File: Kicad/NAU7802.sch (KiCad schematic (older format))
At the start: 19 parts, among them J1 A Scale, J2 B scale, J3 I²C, J4 Scale, J5 AVDD, J6 INT, U1 NAU7802SGI

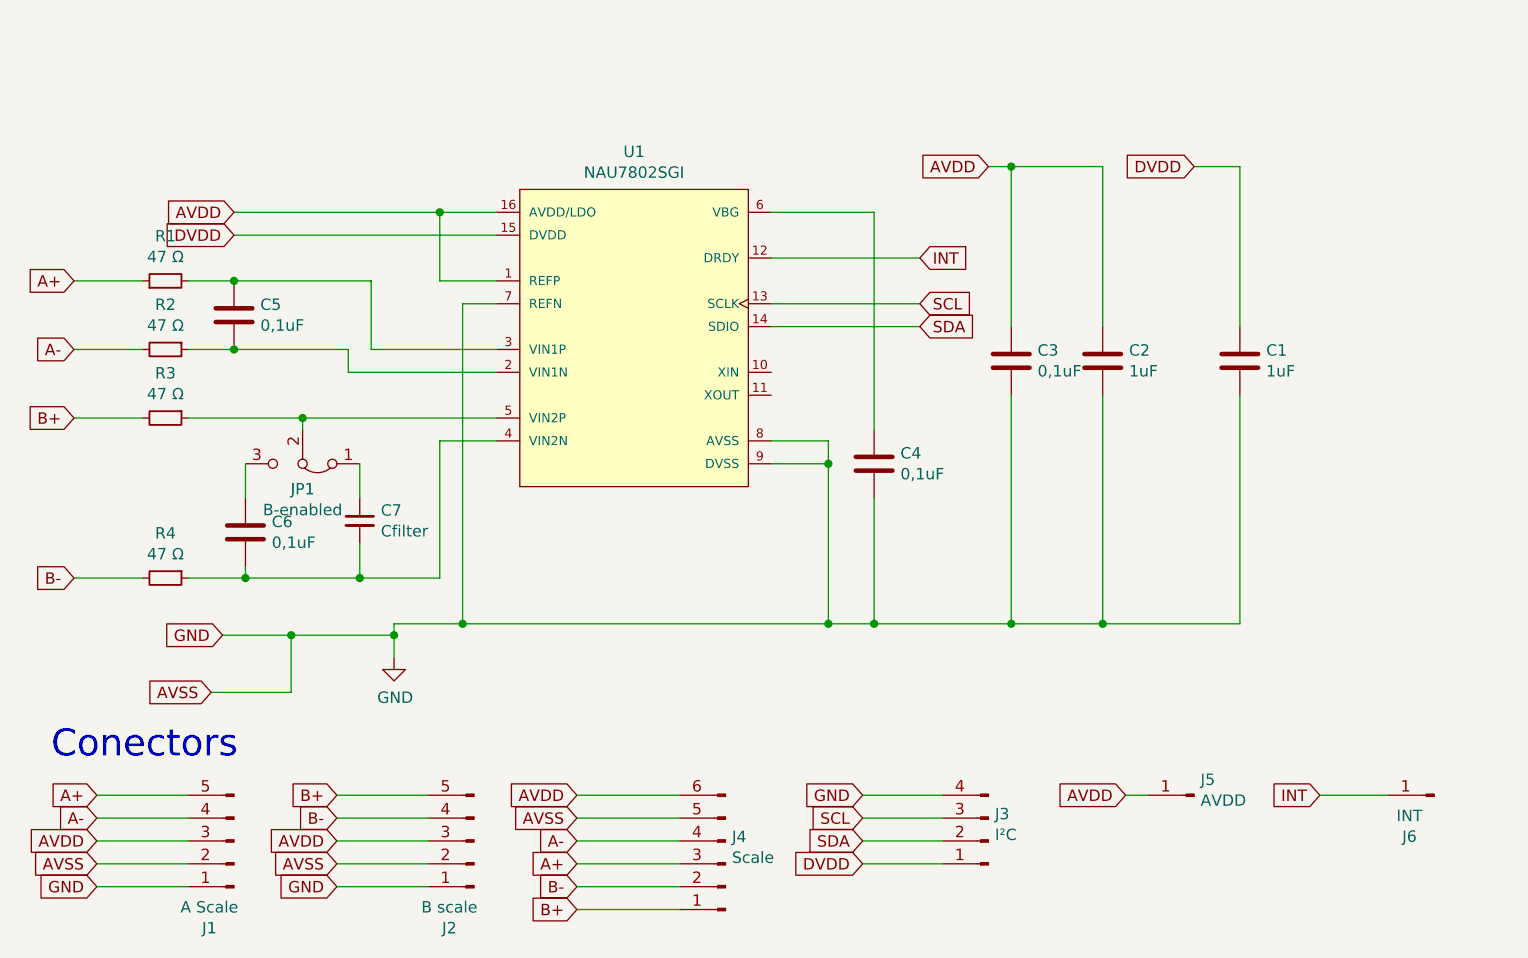
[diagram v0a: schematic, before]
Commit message: ADD I²C Pullup + Jumper
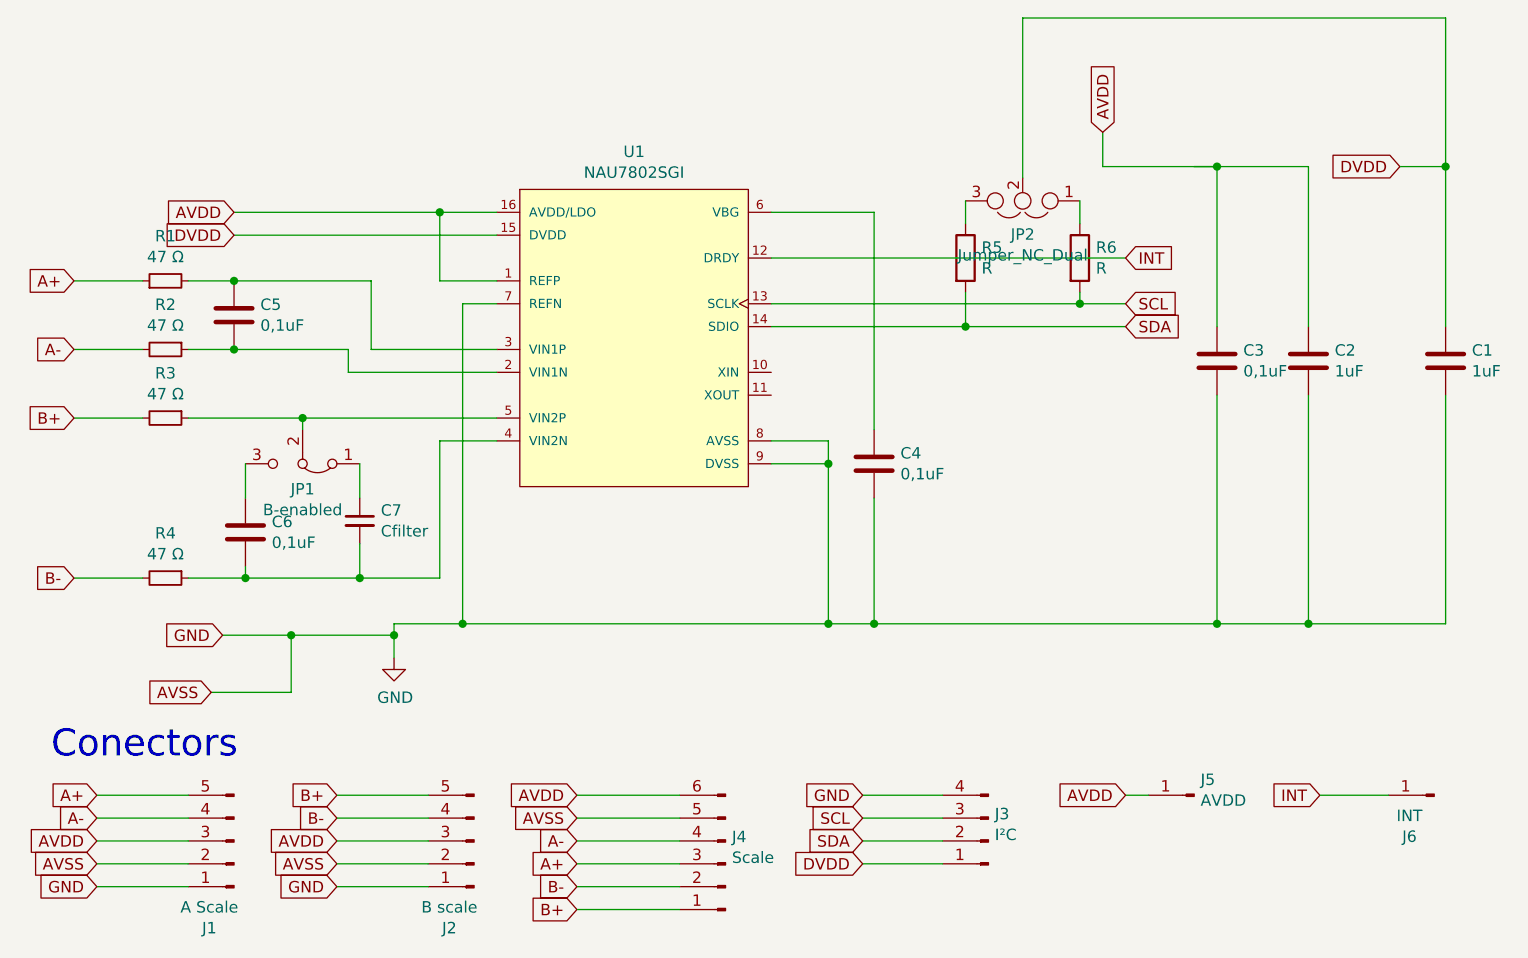
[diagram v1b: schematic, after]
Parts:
- added JP2: Jumper_NC_Dual, Jumper:SolderJumper-3_P1.3mm_Open_RoundedPad1.0x1.5mm, symbol Device:Jumper_NC_Dual
- added R5, R6: R, Resistor_SMD:R_0805_2012Metric, symbol Device:R
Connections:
- net DVDD: now also JP2.2
- net SCL: now also R6.2
- net SDA: now also R5.2
- new net: JP2.1, R6.1
- new net: JP2.3, R5.1
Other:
- moved on the sheet: C1, C2, C3
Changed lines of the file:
@@
 L Device:C C2
 U 1 1 5F00379D
-P 6850 3550
-F 0 "C2" H 6965 3596 50  0000 L CNN
-F 1 "1uF" H 6965 3505 50  0000 L CNN
-F 2 "Capacitor_SMD:C_0805_2012Metric" H 6888 3400 50  0001 C CNN
-F 3 "~" H 6850 3550 50  0001 C CNN
-	1    6850 3550
+P 7750 3550
+F 0 "C2" H 7865 3596 50  0000 L CNN
+F 1 "1uF" H 7865 3505 50  0000 L CNN
+F 2 "Capacitor_SMD:C_0805_2012Metric" H 7788 3400 50  0001 C CNN
+F 3 "~" H 7750 3550 50  0001 C CNN
+	1    7750 3550
 	1    0    0    -1
 $EndComp
@@
 L Device:C C1
 U 1 1 5F003FEF
-P 7450 3550
-F 0 "C1" H 7565 3596 50  0000 L CNN
-F 1 "1uF" H 7565 3505 50  0000 L CNN
-F 2 "Capacitor_SMD:C_0805_2012Metric" H 7488 3400 50  0001 C CNN
-F 3 "~" H 7450 3550 50  0001 C CNN
-	1    7450 3550
+P 8350 3550
+F 0 "C1" H 8465 3596 50  0000 L CNN
+F 1 "1uF" H 8465 3505 50  0000 L CNN
+F 2 "Capacitor_SMD:C_0805_2012Metric" H 8388 3400 50  0001 C CNN
+F 3 "~" H 8350 3550 50  0001 C CNN
+	1    8350 3550
 	1    0    0    -1
 $EndComp
@@
 Wire Wire Line
 	3500 5850 3900 5850
-Text GLabel 6050 3400 2    50   Input ~ 0
+Text GLabel 6950 3400 2    50   Input ~ 0
 SDA
-Text GLabel 6050 3300 2    50   Input ~ 0
+Text GLabel 6950 3300 2    50   Input ~ 0
 SCL
-Text GLabel 6050 3100 2    50   Input ~ 0
+Text GLabel 6950 3100 2    50   Input ~ 0
 INT
 Wire Wire Line
@@
 Wire Wire Line
 	5400 4000 5650 4000
-Wire Wire Line
-	5400 3100 6050 3100
-Wire Wire Line
-	5400 3300 6050 3300
-Wire Wire Line
-	5400 3400 6050 3400
 $Comp
 L Device:C C3
 U 1 1 5F05C52D
-P 6450 3550
-F 0 "C3" H 6565 3596 50  0000 L CNN
-F 1 "0,1uF" H 6565 3505 50  0000 L CNN
-F 2 "Capacitor_SMD:C_0805_2012Metric" H 6488 3400 50  0001 C CNN
-F 3 "~" H 6450 3550 50  0001 C CNN
-	1    6450 3550
-	1    0    0    -1
-$EndComp
-Text GLabel 6350 2700 0    50   Input ~ 0
+P 7350 3550
+F 0 "C3" H 7465 3596 50  0000 L CNN
+F 1 "0,1uF" H 7465 3505 50  0000 L CNN
+F 2 "Capacitor_SMD:C_0805_2012Metric" H 7388 3400 50  0001 C CNN
+F 3 "~" H 7350 3550 50  0001 C CNN
+	1    7350 3550
+	1    0    0    -1
+$EndComp
+Text GLabel 6850 2550 1    50   Input ~ 0
 AVDD
-Text GLabel 7250 2700 0    50   Input ~ 0
+Text GLabel 8150 2700 0    50   Input ~ 0
 DVDD
 Wire Wire Line
-	6350 2700 6450 2700
-Wire Wire Line
-	6450 2700 6450 3400
-Wire Wire Line
-	6850 2700 6850 3400
-Connection ~ 5850 4700
+	7350 2700 7350 3400
+Wire Wire Line
+	7750 2700 7750 3400
 Text GLabel 5800 5750 0    50   Input ~ 0
 DVDD
@@
 Wire Wire Line
 	4550 5950 5000 5950
-Connection ~ 6450 2700
-Connection ~ 6450 4700
-Wire Wire Line
-	5850 4700 6450 4700
-Connection ~ 6850 4700
-Wire Wire Line
-	6450 4700 6850 4700
-Wire Wire Line
-	7250 2700 7450 2700
-Wire Wire Line
-	7450 2700 7450 3400
-Wire Wire Line
-	6450 2700 6850 2700
-Wire Wire Line
-	6850 4700 7450 4700
+Connection ~ 7350 2700
+Connection ~ 7350 4700
+Connection ~ 7750 4700
+Wire Wire Line
+	7350 4700 7750 4700
+Wire Wire Line
+	8150 2700 8350 2700
+Wire Wire Line
+	8350 2700 8350 3400
+Wire Wire Line
+	7350 2700 7750 2700
+Wire Wire Line
+	7750 4700 8350 4700
 Wire Wire Line
 	3050 3000 4200 3000
@@
 Connection ~ 5650 4000
 Wire Wire Line
-	6450 3700 6450 4700
-Wire Wire Line
-	6850 3700 6850 4700
-Wire Wire Line
-	7450 3700 7450 4700
+	7350 3700 7350 4700
+Wire Wire Line
+	7750 3700 7750 4700
+Wire Wire Line
+	8350 3700 8350 4700
 Wire Wire Line
 	4050 4700 5650 4700
@@
 Wire Wire Line
 	3350 3800 4200 3800
+Wire Wire Line
+	5850 4700 7350 4700
+Connection ~ 5850 4700
+Wire Wire Line
+	5400 3100 6950 3100
+$Comp
+L Device:Jumper_NC_Dual JP2
+U 1 1 5F0512F0
+P 6500 2850
+F 0 "JP2" H 6500 2997 50  0000 C CNN
+F 1 "Jumper_NC_Dual" H 6500 3088 50  0000 C CNN
+F 2 "Jumper:SolderJumper-3_P1.3mm_Open_RoundedPad1.0x1.5mm" H 6500 2850 50  0001 C CNN
+F 3 "~" H 6500 2850 50  0001 C CNN
+	1    6500 2850
+	-1   0    0    1
+$EndComp
+Wire Wire Line
+	6500 2750 6500 2050
+Wire Wire Line
+	6500 2050 8350 2050
+Wire Wire Line
+	8350 2050 8350 2700
+Connection ~ 8350 2700
+Wire Wire Line
+	6850 2550 6850 2700
+$Comp
+L Device:R R5
+U 1 1 5F05ACB5
+P 6250 3100
+F 0 "R5" H 6320 3146 50  0000 L CNN
+F 1 "R" H 6320 3055 50  0000 L CNN
+F 2 "Resistor_SMD:R_0805_2012Metric" V 6180 3100 50  0001 C CNN
+F 3 "~" H 6250 3100 50  0001 C CNN
+	1    6250 3100
+	1    0    0    -1
+$EndComp
+$Comp
+L Device:R R6
+U 1 1 5F05BCD1
+P 6750 3100
+F 0 "R6" H 6820 3146 50  0000 L CNN
+F 1 "R" H 6820 3055 50  0000 L CNN
+F 2 "Resistor_SMD:R_0805_2012Metric" V 6680 3100 50  0001 C CNN
+F 3 "~" H 6750 3100 50  0001 C CNN
+	1    6750 3100
+	1    0    0    -1
+$EndComp
+Wire Wire Line
+	5400 3300 6750 3300
+Wire Wire Line
+	6250 2850 6250 2950
+Wire Wire Line
+	7250 2700 7350 2700
+Wire Wire Line
+	6850 2700 7350 2700
+Wire Wire Line
+	6750 2850 6750 2950
+Wire Wire Line
+	6250 3250 6250 3400
+Wire Wire Line
+	5400 3400 6250 3400
+Wire Wire Line
+	6750 3250 6750 3300
+Connection ~ 6750 3300
+Wire Wire Line
+	6750 3300 6950 3300
+Wire Wire Line
+	6250 3400 6950 3400
+Connection ~ 6250 3400
 $EndSCHEMATC
